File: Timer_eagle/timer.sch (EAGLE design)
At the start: 22 parts, among them IC1 NE555, IC2 4081N, IC3 4518N, IC4 4070N, IC5 4070N, K1 G5L, Q1 BC548, Q2 TIP120, X1 SSW-103-02-S-S

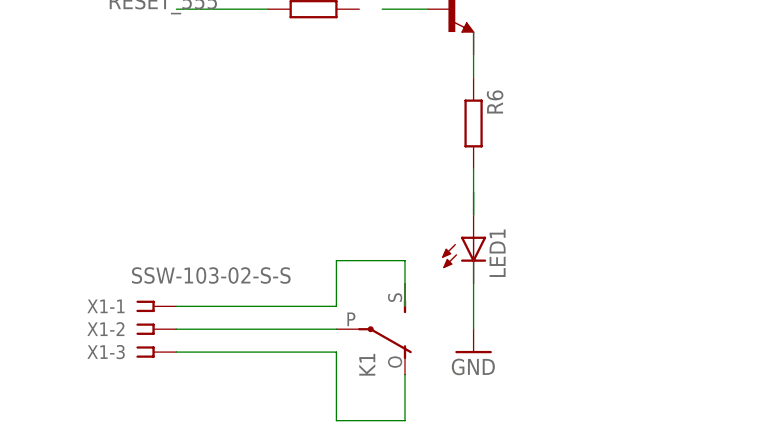
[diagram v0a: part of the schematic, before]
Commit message: Alguns erros no esquemático foram consertados
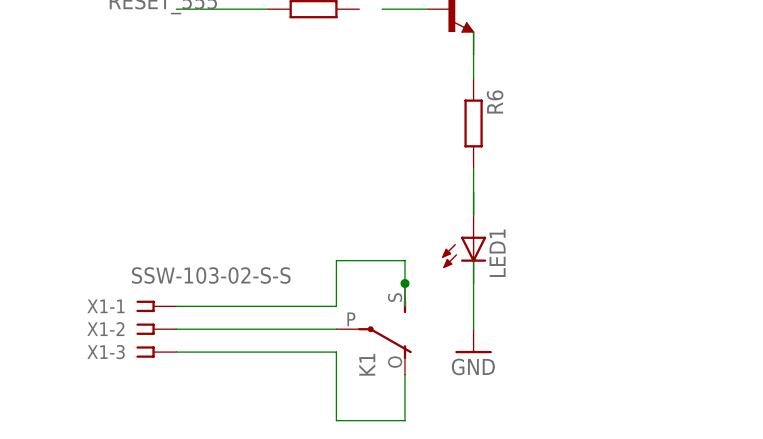
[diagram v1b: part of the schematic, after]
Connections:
- net N$20: now also K12.S
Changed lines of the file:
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@@
 <wire x1="137.16" y1="50.8" x2="137.16" y2="55.88" width="0.1524" layer="91"/>
 <wire x1="137.16" y1="55.88" x2="144.78" y2="55.88" width="0.1524" layer="91"/>
-<wire x1="144.78" y1="55.88" x2="144.78" y2="50.8" width="0.1524" layer="91"/>
+<wire x1="144.78" y1="55.88" x2="144.78" y2="53.34" width="0.1524" layer="91"/>
+<pinref part="K1" gate="2" pin="S"/>
+<wire x1="144.78" y1="53.34" x2="144.78" y2="50.8" width="0.1524" layer="91"/>
+<junction x="144.78" y="53.34"/>
 </segment>
 </net>

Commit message: O projeto da plva está atualizado
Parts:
- removed IC5: 4070N, 40xx:4070N
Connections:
- net GND: now also LED1.C
- net N$13: no longer IC5C.I1
- net N$14: no longer IC5C.O
- net N$16: now also Q2.C
- net N$19: now also X1-1.1; no longer X1-2.1
- net N$20: now also X1-2.1; no longer X1-1.1
- net N$22: now also R5.2
- net N$24: now also Q1.E
- net VCC: no longer IC5C.I0
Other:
- moved on the sheet: IC4C, LED1
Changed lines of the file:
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@@
 <part name="C2" library="resistor" deviceset="C-EU" device="025-024X044"/>
 <part name="P+4" library="supply1" deviceset="VCC" device=""/>
-<part name="IC5" library="40xx" deviceset="4070" device="N"/>
 <part name="SV1" library="con-lstb" deviceset="MA04-1" device=""/>
 <part name="P+5" library="supply1" deviceset="VCC" device=""/>
@@
 <instance part="IC4" gate="A" x="132.08" y="142.24"/>
 <instance part="IC4" gate="B" x="132.08" y="127"/>
-<instance part="IC4" gate="C" x="132.08" y="111.76"/>
+<instance part="IC4" gate="C" x="134.62" y="114.3"/>
 <instance part="K1" gate="1" x="83.82" y="78.74"/>
 <instance part="K1" gate="2" x="139.7" y="48.26" rot="R270"/>
@@
 <instance part="C1" gate="G$1" x="0" y="116.84"/>
 <instance part="D1" gate="1" x="96.52" y="78.74" rot="R90"/>
-<instance part="LED1" gate="G$1" x="152.4" y="58.42"/>
+<instance part="LED1" gate="G$1" x="152.4" y="60.96"/>
 <instance part="Q1" gate="G$1" x="149.86" y="83.82"/>
 <instance part="Q2" gate="1" x="81.28" y="66.04"/>
@@
 <instance part="C2" gate="G$1" x="35.56" y="127"/>
 <instance part="P+4" gate="VCC" x="111.76" y="157.48"/>
-<instance part="IC5" gate="C" x="132.08" y="111.76"/>
 <instance part="SV1" gate="1" x="170.18" y="142.24" rot="R180"/>
 <instance part="P+5" gate="VCC" x="83.82" y="91.44"/>
@@
 <wire x1="38.1" y1="88.9" x2="33.02" y2="88.9" width="0.1524" layer="91"/>
 <wire x1="33.02" y1="88.9" x2="33.02" y2="99.06" width="0.1524" layer="91"/>
+<junction x="33.02" y="99.06"/>
+<junction x="40.64" y="116.84"/>
+<junction x="22.86" y="99.06"/>
+<junction x="27.94" y="99.06"/>
 </segment>
 <segment>
@@
 <pinref part="C2" gate="G$1" pin="2"/>
 <wire x1="35.56" y1="121.92" x2="30.48" y2="121.92" width="0.1524" layer="91"/>
+<junction x="30.48" y="121.92"/>
 </segment>
 <segment>
@@
 <pinref part="GND5" gate="1" pin="GND"/>
 <wire x1="152.4" y1="48.26" x2="152.4" y2="55.88" width="0.1524" layer="91"/>
+<pinref part="LED1" gate="G$1" pin="C"/>
 </segment>
 </net>
@@
 <wire x1="0" y1="119.38" x2="0" y2="121.92" width="0.1524" layer="91"/>
 <wire x1="7.62" y1="119.38" x2="0" y2="119.38" width="0.1524" layer="91"/>
+<junction x="0" y="119.38"/>
+<junction x="7.62" y="127"/>
 </segment>
 </net>
@@
 <wire x1="0" y1="134.62" x2="0" y2="132.08" width="0.1524" layer="91"/>
 <wire x1="10.16" y1="134.62" x2="0" y2="134.62" width="0.1524" layer="91"/>
+<junction x="0" y="134.62"/>
 </segment>
 </net>
@@
 <wire x1="30.48" y1="142.24" x2="27.94" y2="142.24" width="0.1524" layer="91"/>
 <junction x="30.48" y="142.24"/>
+<junction x="0" y="149.86"/>
 </segment>
 <segment>
@@
 <wire x1="111.76" y1="129.54" x2="111.76" y2="144.78" width="0.1524" layer="91"/>
 <pinref part="IC4" gate="C" pin="I0"/>
-<pinref part="IC5" gate="C" pin="I0"/>
-<wire x1="124.46" y1="114.3" x2="111.76" y2="114.3" width="0.1524" layer="91"/>
-<wire x1="111.76" y1="114.3" x2="111.76" y2="129.54" width="0.1524" layer="91"/>
+<wire x1="127" y1="116.84" x2="111.76" y2="116.84" width="0.1524" layer="91"/>
+<wire x1="111.76" y1="116.84" x2="111.76" y2="129.54" width="0.1524" layer="91"/>
 <junction x="111.76" y="144.78"/>
 <junction x="111.76" y="129.54"/>
@@
 <pinref part="Q1" gate="G$1" pin="C"/>
 <wire x1="152.4" y1="93.98" x2="152.4" y2="88.9" width="0.1524" layer="91"/>
+<junction x="83.82" y="86.36"/>
+<junction x="96.52" y="86.36"/>
 </segment>
 </net>
@@
 <wire x1="50.8" y1="91.44" x2="45.72" y2="91.44" width="0.1524" layer="91"/>
 <wire x1="45.72" y1="91.44" x2="45.72" y2="109.22" width="0.1524" layer="91"/>
+<wire x1="45.72" y1="109.22" x2="48.26" y2="109.22" width="0.1524" layer="91"/>
+<wire x1="48.26" y1="109.22" x2="48.26" y2="127" width="0.1524" layer="91"/>
+<junction x="45.72" y="109.22"/>
+<wire x1="48.26" y1="127" x2="45.72" y2="127" width="0.1524" layer="91"/>
 <pinref part="IC3" gate="A" pin="RES"/>
-<wire x1="45.72" y1="109.22" x2="45.72" y2="129.54" width="0.1524" layer="91"/>
+<wire x1="45.72" y1="127" x2="45.72" y2="129.54" width="0.1524" layer="91"/>
 </segment>
 </net>
@@
 <segment>
 <pinref part="IC4" gate="C" pin="I1"/>
-<pinref part="IC5" gate="C" pin="I1"/>
 <pinref part="IC2" gate="C" pin="O"/>
 <wire x1="101.6" y1="104.14" x2="119.38" y2="104.14" width="0.1524" layer="91"/>
-<wire x1="119.38" y1="104.14" x2="119.38" y2="109.22" width="0.1524" layer="91"/>
-<wire x1="119.38" y1="109.22" x2="124.46" y2="109.22" width="0.1524" layer="91"/>
+<wire x1="119.38" y1="104.14" x2="119.38" y2="111.76" width="0.1524" layer="91"/>
+<wire x1="119.38" y1="111.76" x2="127" y2="111.76" width="0.1524" layer="91"/>
 </segment>
 </net>
@@
 <segment>
 <pinref part="IC4" gate="C" pin="O"/>
-<pinref part="IC5" gate="C" pin="O"/>
-<wire x1="139.7" y1="111.76" x2="160.02" y2="111.76" width="0.1524" layer="91"/>
+<wire x1="142.24" y1="99.06" x2="160.02" y2="111.76" width="0.1524" layer="91"/>
 <wire x1="160.02" y1="111.76" x2="160.02" y2="142.24" width="0.1524" layer="91"/>
 <pinref part="SV1" gate="1" pin="3"/>
 <wire x1="160.02" y1="142.24" x2="162.56" y2="142.24" width="0.1524" layer="91"/>
+<wire x1="142.24" y1="99.06" x2="142.24" y2="114.3" width="0.1524" layer="91"/>
 </segment>
 </net>
@@
 <pinref part="D1" gate="1" pin="A"/>
 <wire x1="96.52" y1="71.12" x2="96.52" y2="76.2" width="0.1524" layer="91"/>
-</segment>
-</net>
-<net name="N$19" class="0">
-<segment>
-<pinref part="X1" gate="-2" pin="1"/>
-<pinref part="K1" gate="2" pin="P"/>
-<wire x1="119.38" y1="48.26" x2="137.16" y2="48.26" width="0.1524" layer="91"/>
+<pinref part="Q2" gate="1" pin="C"/>
+<junction x="83.82" y="71.12"/>
 </segment>
 </net>
 <net name="N$20" class="0">
 <segment>
-<pinref part="X1" gate="-1" pin="1"/>
-<wire x1="119.38" y1="50.8" x2="137.16" y2="50.8" width="0.1524" layer="91"/>
 <wire x1="137.16" y1="50.8" x2="137.16" y2="55.88" width="0.1524" layer="91"/>
 <wire x1="137.16" y1="55.88" x2="144.78" y2="55.88" width="0.1524" layer="91"/>
@@
 <wire x1="144.78" y1="53.34" x2="144.78" y2="50.8" width="0.1524" layer="91"/>
 <junction x="144.78" y="53.34"/>
+<wire x1="137.16" y1="50.8" x2="129.54" y2="50.8" width="0.1524" layer="91"/>
+<wire x1="129.54" y1="50.8" x2="129.54" y2="48.26" width="0.1524" layer="91"/>
+<pinref part="X1" gate="-2" pin="1"/>
+<wire x1="129.54" y1="48.26" x2="119.38" y2="48.26" width="0.1524" layer="91"/>
 </segment>
 </net>
@@
 </segment>
 </net>
+<net name="N$23" class="0">
+<segment>
+<pinref part="LED1" gate="G$1" pin="A"/>
+<pinref part="R6" gate="G$1" pin="2"/>
+<wire x1="152.4" y1="63.5" x2="152.4" y2="66.04" width="0.1524" layer="91"/>
+</segment>
+</net>
+<net name="N$24" class="0">
+<segment>
+<pinref part="R6" gate="G$1" pin="1"/>
+<wire x1="152.4" y1="76.2" x2="152.4" y2="78.74" width="0.1524" layer="91"/>
+<pinref part="Q1" gate="G$1" pin="E"/>
+</segment>
+</net>
 <net name="N$22" class="0">
 <segment>
 <pinref part="Q1" gate="G$1" pin="B"/>
-<wire x1="142.24" y1="83.82" x2="147.32" y2="83.82" width="0.1524" layer="91"/>
-</segment>
-</net>
-<net name="N$23" class="0">
-<segment>
-<pinref part="LED1" gate="G$1" pin="A"/>
-<wire x1="152.4" y1="60.96" x2="152.4" y2="63.5" width="0.1524" layer="91"/>
-<pinref part="R6" gate="G$1" pin="2"/>
-<wire x1="152.4" y1="60.96" x2="152.4" y2="66.04" width="0.1524" layer="91"/>
-</segment>
-</net>
-<net name="N$24" class="0">
-<segment>
-<pinref part="R6" gate="G$1" pin="1"/>
-<wire x1="152.4" y1="76.2" x2="152.4" y2="81.28" width="0.1524" layer="91"/>
-</segment>
-</net>
+<wire x1="137.16" y1="83.82" x2="139.7" y2="83.82" width="0.1524" layer="91"/>
+<pinref part="R5" gate="G$1" pin="2"/>
+<wire x1="139.7" y1="83.82" x2="147.32" y2="83.82" width="0.1524" layer="91"/>
+<junction x="139.7" y="83.82"/>
+</segment>
+</net>
+<net name="N$19" class="0">
+<segment>
+<pinref part="K1" gate="2" pin="P"/>
+<wire x1="137.16" y1="48.26" x2="132.08" y2="48.26" width="0.1524" layer="91"/>
+<wire x1="132.08" y1="48.26" x2="132.08" y2="53.34" width="0.1524" layer="91"/>
+<wire x1="132.08" y1="53.34" x2="119.38" y2="53.34" width="0.1524" layer="91"/>
+<pinref part="X1" gate="-1" pin="1"/>
+<wire x1="119.38" y1="53.34" x2="119.38" y2="50.8" width="0.1524" layer="91"/>
+</segment>
+</net>

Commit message: Projeto final da placa
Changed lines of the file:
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@@
 <part name="R6" library="eagle-ltspice" deviceset="R" device="0207/10"/>
 <part name="GND5" library="supply1" deviceset="GND" device=""/>
+<part name="VSS1" library="supply1" deviceset="VSS" device=""/>
 </parts>
 <sheets>
@@
 <instance part="R6" gate="G$1" x="152.4" y="71.12" rot="R270"/>
 <instance part="GND5" gate="1" x="152.4" y="45.72"/>
+<instance part="VSS1" gate="G$1" x="30.48" y="91.44"/>
 </instances>
 <busses>
@@
 <wire x1="40.64" y1="99.06" x2="33.02" y2="99.06" width="0.1524" layer="91"/>
 <pinref part="R1" gate="G$1" pin="1"/>
-<wire x1="33.02" y1="99.06" x2="27.94" y2="99.06" width="0.1524" layer="91"/>
+<wire x1="33.02" y1="99.06" x2="30.48" y2="99.06" width="0.1524" layer="91"/>
+<wire x1="30.48" y1="99.06" x2="27.94" y2="99.06" width="0.1524" layer="91"/>
 <wire x1="38.1" y1="88.9" x2="33.02" y2="88.9" width="0.1524" layer="91"/>
 <wire x1="33.02" y1="88.9" x2="33.02" y2="99.06" width="0.1524" layer="91"/>
@@
 <junction x="22.86" y="99.06"/>
 <junction x="27.94" y="99.06"/>
+<pinref part="VSS1" gate="G$1" pin="VSS"/>
+<wire x1="30.48" y1="93.98" x2="30.48" y2="99.06" width="0.1524" layer="91"/>
+<junction x="30.48" y="99.06"/>
 </segment>
 <segment>

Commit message: Esquemático Corrigido (Ligação RES_555) Projeto da Placa refeito
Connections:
- new net Q3_EN2: IC3A.Q3, IC3B.EN
- net RESET_555: no longer IC3A.Q3, IC3B.EN
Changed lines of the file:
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@@
-</segment>
-<segment>
-<pinref part="IC3" gate="A" pin="Q3"/>
-<wire x1="71.12" y1="129.54" x2="71.12" y2="121.92" width="0.1524" layer="91"/>
-<wire x1="71.12" y1="121.92" x2="43.18" y2="121.92" width="0.1524" layer="91"/>
-<wire x1="43.18" y1="121.92" x2="43.18" y2="114.3" width="0.1524" layer="91"/>
-<pinref part="IC3" gate="B" pin="EN"/>
-<wire x1="43.18" y1="114.3" x2="45.72" y2="114.3" width="0.1524" layer="91"/>
 </segment>
 <segment>
@@
 </segment>
 </net>
+<net name="Q3_EN2" class="0">
+<segment>
+<pinref part="IC3" gate="A" pin="Q3"/>
+<wire x1="71.12" y1="129.54" x2="71.12" y2="121.92" width="0.1524" layer="91"/>
+<wire x1="71.12" y1="121.92" x2="43.18" y2="121.92" width="0.1524" layer="91"/>
+<wire x1="43.18" y1="121.92" x2="43.18" y2="114.3" width="0.1524" layer="91"/>
+<pinref part="IC3" gate="B" pin="EN"/>
+<wire x1="43.18" y1="114.3" x2="45.72" y2="114.3" width="0.1524" layer="91"/>
+</segment>
+</net>
